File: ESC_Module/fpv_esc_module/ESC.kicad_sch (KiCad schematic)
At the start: 25 parts, among them U203 STM32F051K8, U204 STM32F051K8Ux, U25 FD6288Q

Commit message: MCU Sybole made
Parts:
- added C202: 0.1u, Capacitor_SMD:C_0402_1005Metric, symbol Device:C
- added R203: 10K, Resistor_SMD:R_0402_1005Metric, symbol Device:R
- R14, R15, R16: value 1K -> 10K; manf# ERJ-2RKF1001X -> (none)
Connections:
- net +3V3: now also U203.1 (VDD), U203.17 (VDD), U203.5 (VDDA)
- net BOOT0: now also U203.31 (BOOT0), R203.1
- net GATE_AL: now also U203.15 (PB1)
- net GATE_BL: now also U203.14 (PB0)
- net GND: now also U203.16 (GND), U203.32 (GND), U203.33 (GND), C202.1, R203.2
- net NRST: now also U203.4 (NRST), C202.2
- net TELEMETRY_RX: now also U203.30 (PB7)
- net TELEMETRY_TX: now also U203.29 (PB6)
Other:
- note removed: "Change to 10Ks"
- moved on the sheet: C5, U203C

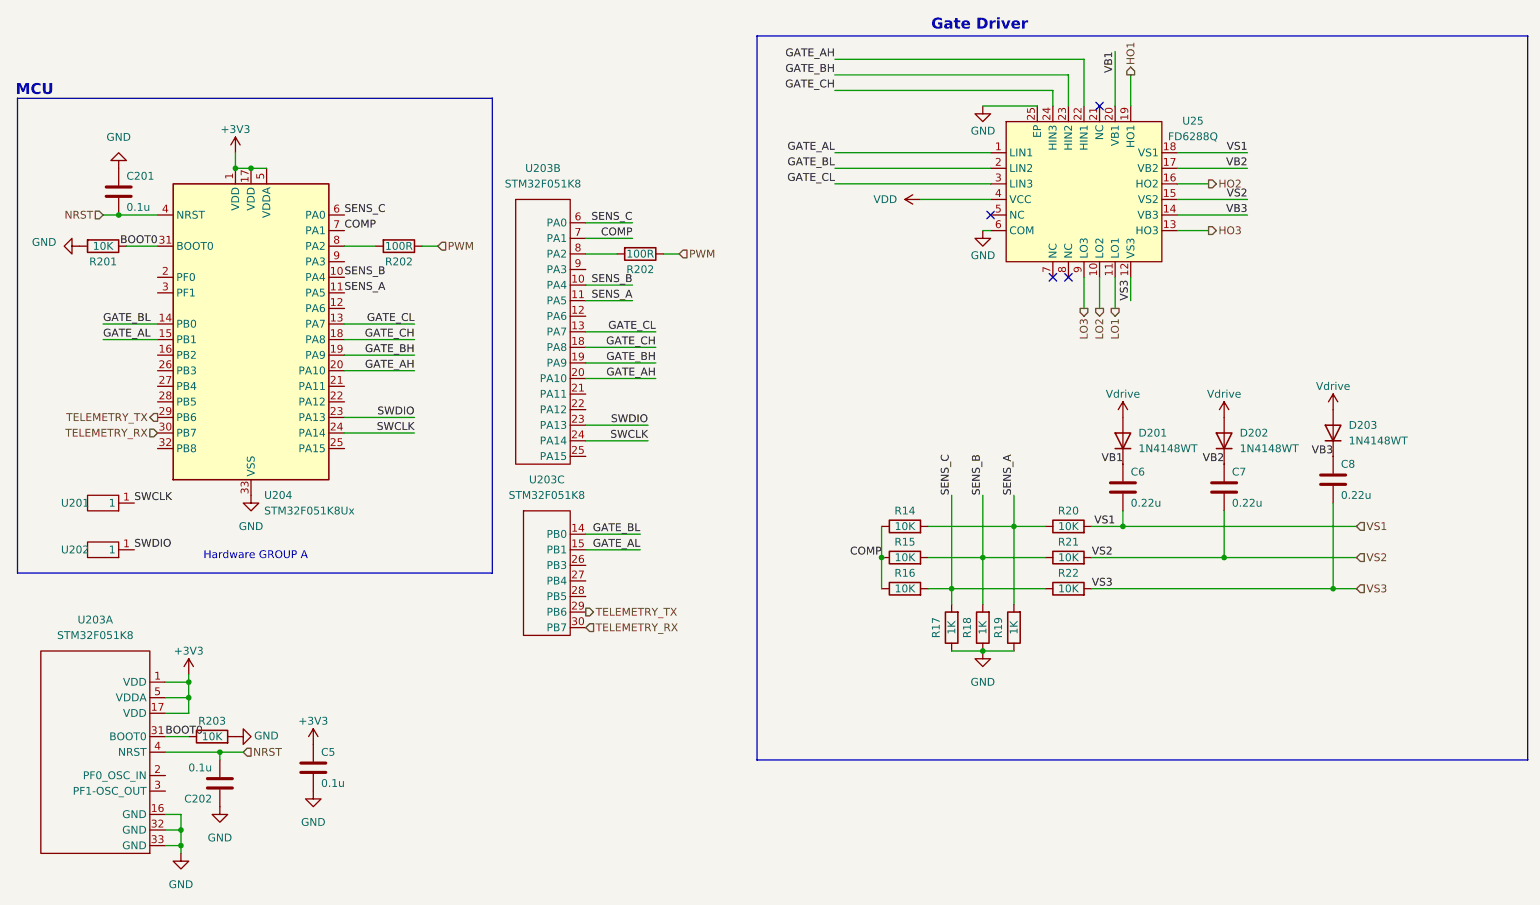
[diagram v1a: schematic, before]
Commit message: Schematic changes made
Made changes to the schematic just starting routing
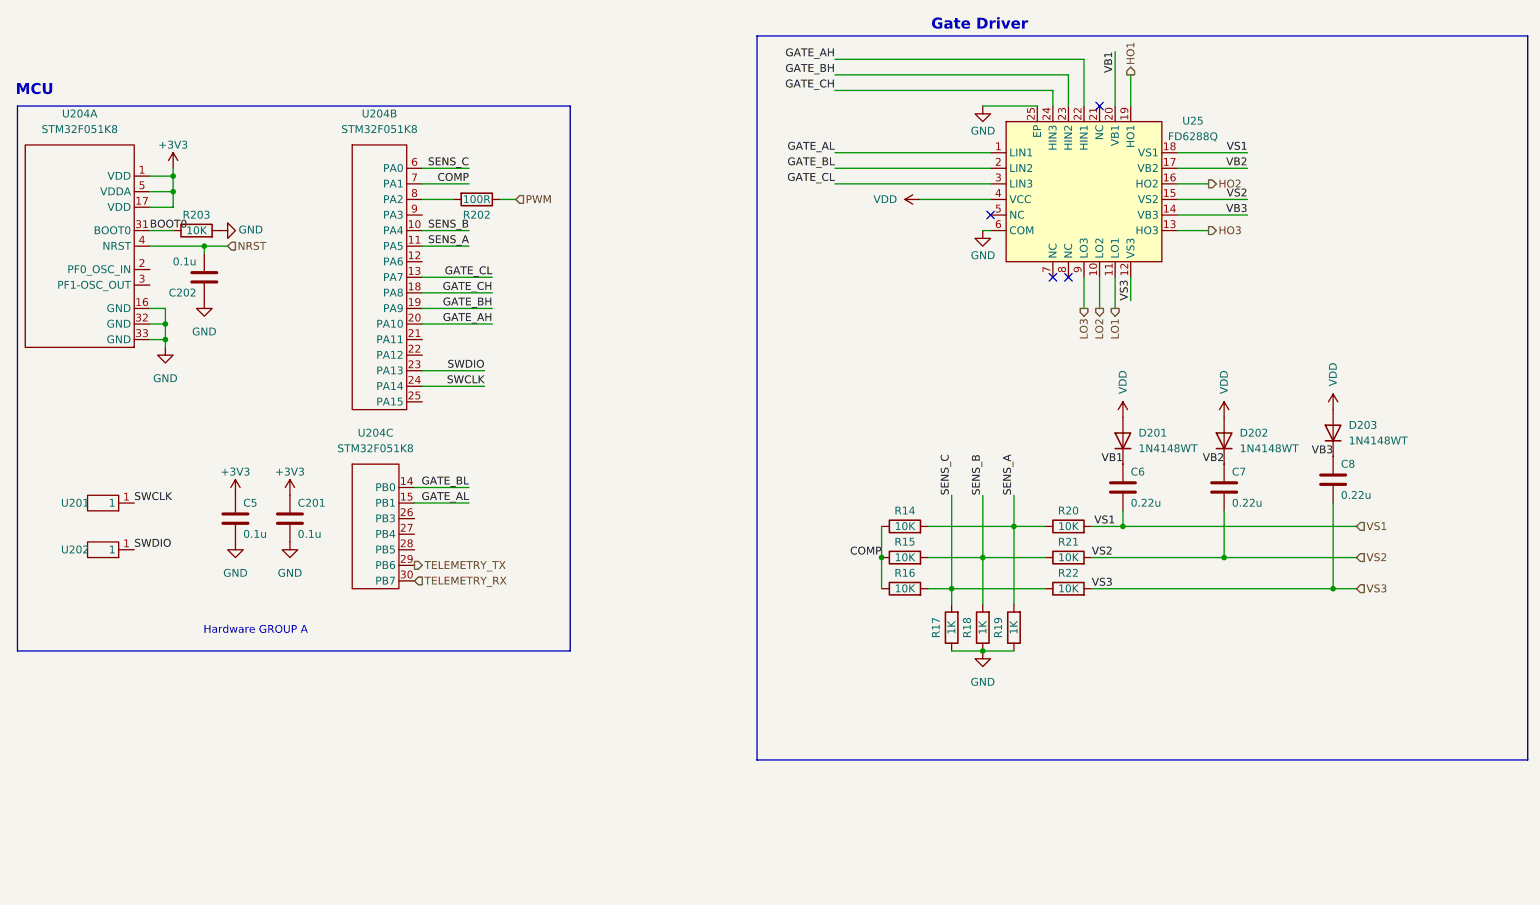
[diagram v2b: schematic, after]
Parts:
- removed R201: 10K, Resistor_SMD:R_0402_1005Metric, symbol Device:R
- removed R202: 100R, Resistor_SMD:R_0402_1005Metric, symbol Device:R
- removed U204: STM32F051K8Ux, Package_DFN_QFN:QFN-32-1EP_5x5mm_P0.5mm_EP3.45x3.45mm, symbol MCU_ST_STM32F0:STM32F051K8Ux
- C6, C7, C8: footprint Capacitor_SMD:C_0603_1608Metric -> Capacitor_SMD:C_0402_1005Metric; digikey# 445-5191-1-ND -> (none); manf TDK Corporation -> (none); manf# GCM188R71H224KA64J -> GRM155R61H224KE01J
- renumbered U203 to U204
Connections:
- net Vdrive is gone; now on net VDD: D201.2 (A), D202.2 (A), D203.2 (A)
- net +3V3: now also C201.1
- net GND: now also C201.2; no longer C201.1
- net NRST: no longer C201.2
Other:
- moved on the sheet: C202, C5, R202, R203, U204A, U204B, U204C
